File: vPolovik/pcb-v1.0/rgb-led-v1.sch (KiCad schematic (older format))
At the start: 11 parts, among them CON1 BARREL_JACK, SW1 SPST

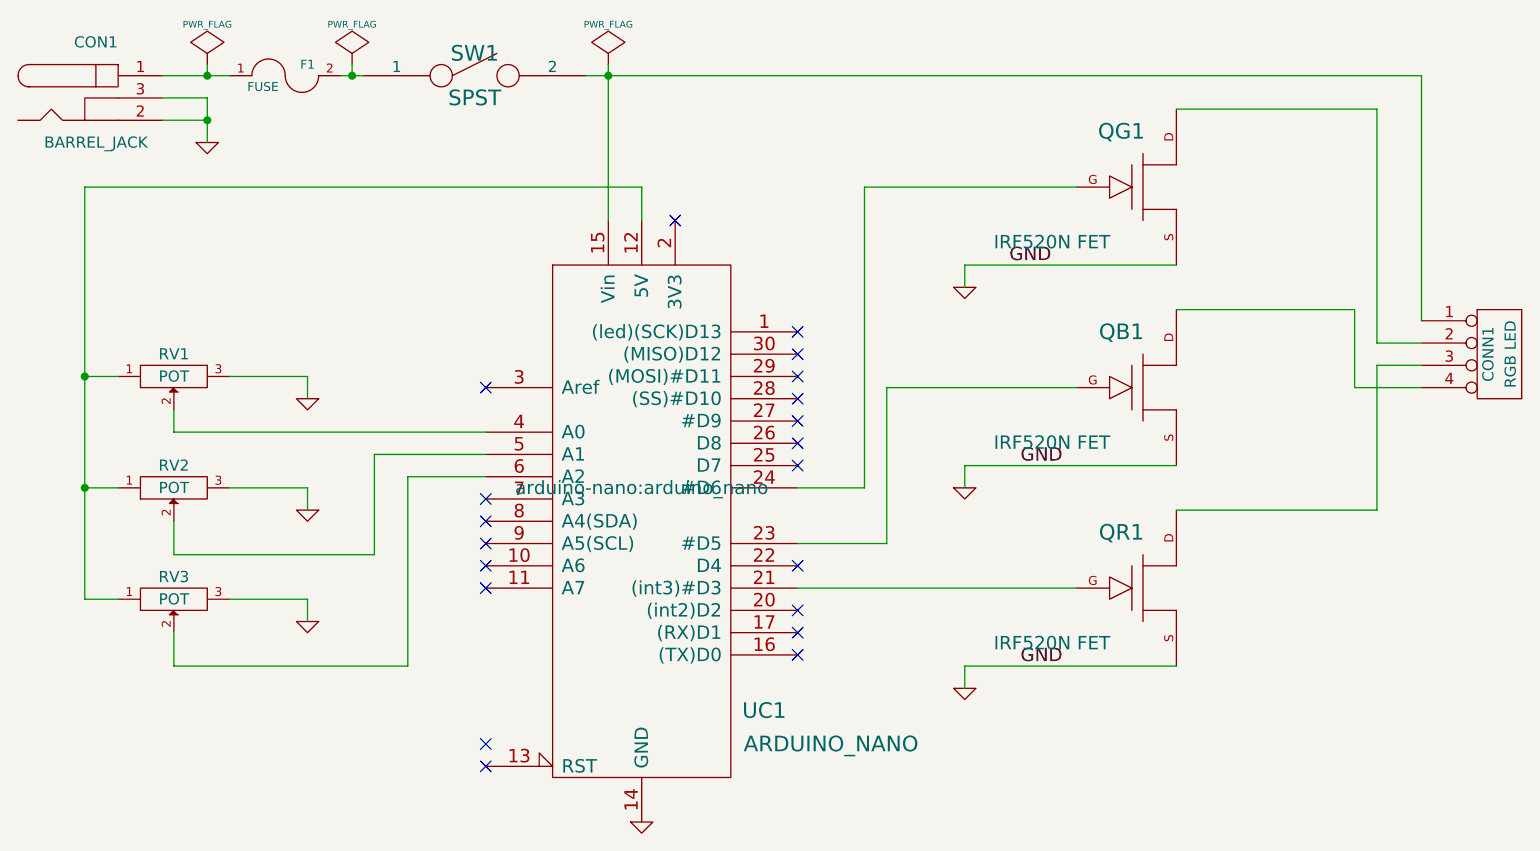
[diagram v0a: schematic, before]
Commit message: Change schematic according to my modification.
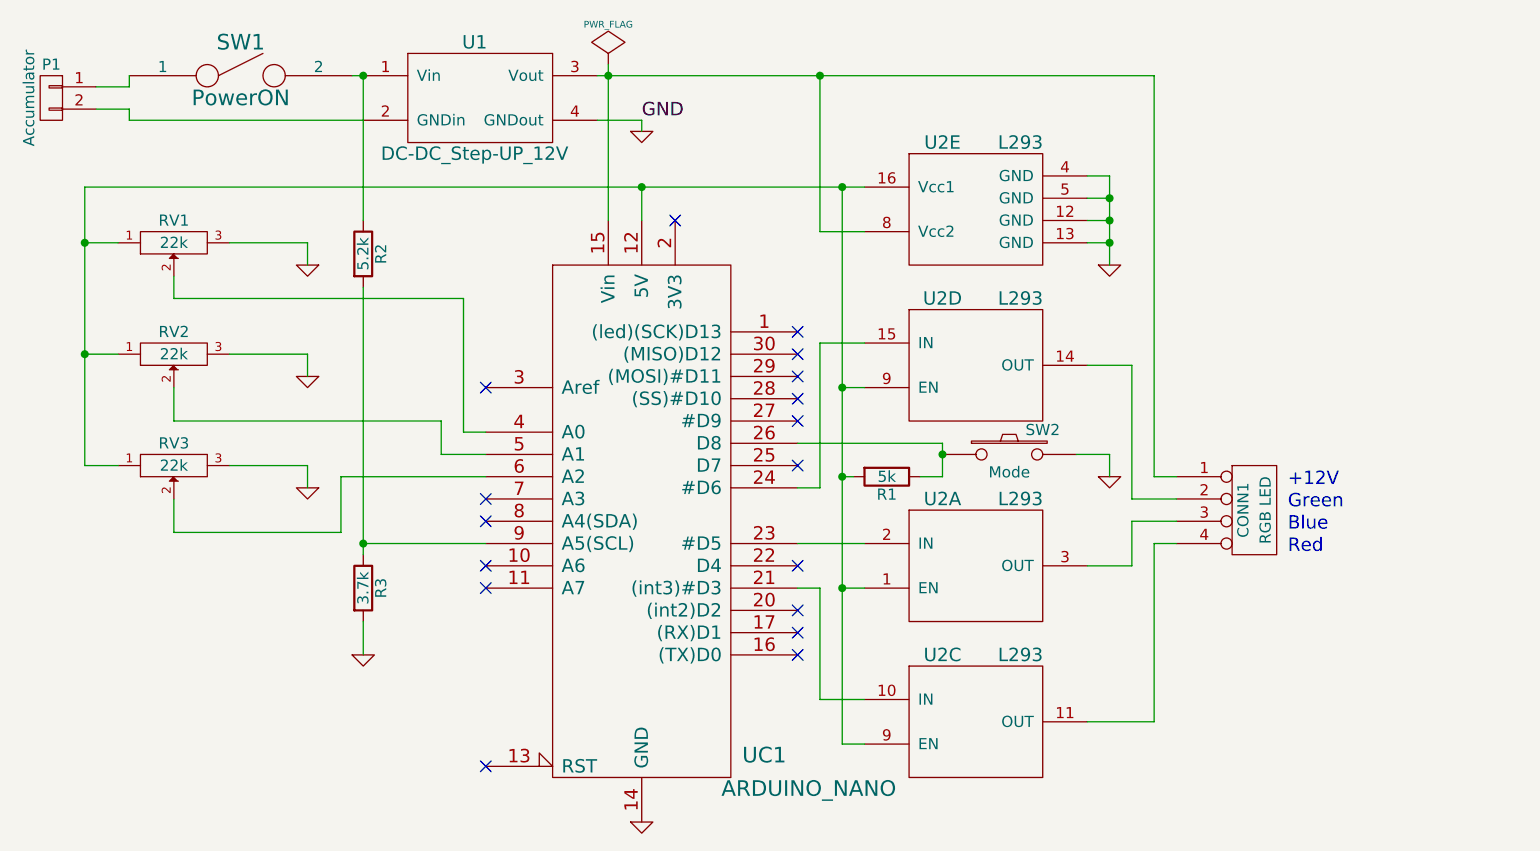
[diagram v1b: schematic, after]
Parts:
- removed CON1: BARREL_JACK, Connect:BARREL_JACK, symbol BARREL_JACK
- removed F1: FUSE, library:KCD3, symbol FUSE
- removed QB1, QG1, QR1: IRF520N FET, library:IRF520N, symbol FET_N
- added P1: Accumulator, symbol CONN_01X02
- added R1: 5k, symbol R
- added R2: 5.2k, symbol R
- added R3: 3.7k, symbol R
- added SW2: Mode, symbol SW_PUSH
- added U1: DC-DC_Step-UP_12V, symbol DC-DC_Step-UP_12V
- added U2: L293, symbol L293
- RV1, RV2, RV3: value POT -> 22k
- SW1: value SPST -> PowerON
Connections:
- net GND: now also R3.2, SW2.2, U1.4 (GNDout), U2.12 (GND), U2.13 (GND), U2.4 (GND), U2.5 (GND)
- net at CONN1.3 (P3): now also U2.3 (OUT)
- net at UC1.21 ((int3)#D3): now also U2.10 (IN)
- net at CONN1.2 (P2): now also U2.14 (OUT)
- net at UC1.24 (#D6): now also U2.15 (IN)
- net at CONN1.4 (P4): now also U2.11 (OUT)
- net at UC1.23 (#D5): now also U2.2 (IN)
- net at CONN1.1 (P1), UC1.15 (Vin): now also U1.3 (Vout), U2.8 (Vcc2); no longer SW1.2
- net at RV1.1, RV2.1, RV3.1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: now also R1.2, U2.1 (EN), U2.16 (Vcc1), U2.9 (EN), U2.9 (EN)
- net at UC1.26 (D8): now also R1.1, SW2.1
- net at UC1.9 (A5(SCL)): now also R2.2, R3.1
- net at SW1.1: now also P1.1 (P1)
- new net: R2.1, SW1.2, U1.1 (Vin)
- new net: P1.2 (P2), U1.2 (GNDin)
- no-connect marks 20 -> 17
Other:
- note added: "+12V"
- note added: "Blue"
- note added: "Green"
- note added: "Red"
- moved on the sheet: CONN1, RV1, RV2, RV3, SW1
